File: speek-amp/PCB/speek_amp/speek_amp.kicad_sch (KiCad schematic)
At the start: 71 parts, among them J1 Conn_01x02, J2 R_Tweeter, J3 R_Woofer, J5 L_Tweeter, J6 L_Sub, J7 L_Woofer, U1 TPA3116D2DAD_C2865736, U2 10uH, U3 10uH, U4 XT60, U5 10uH, U6 10uH, U7 PDMTAT068125-151MLU, U8 PDMTAT068125-151MLU, U9 25PX4700MEFC16X25

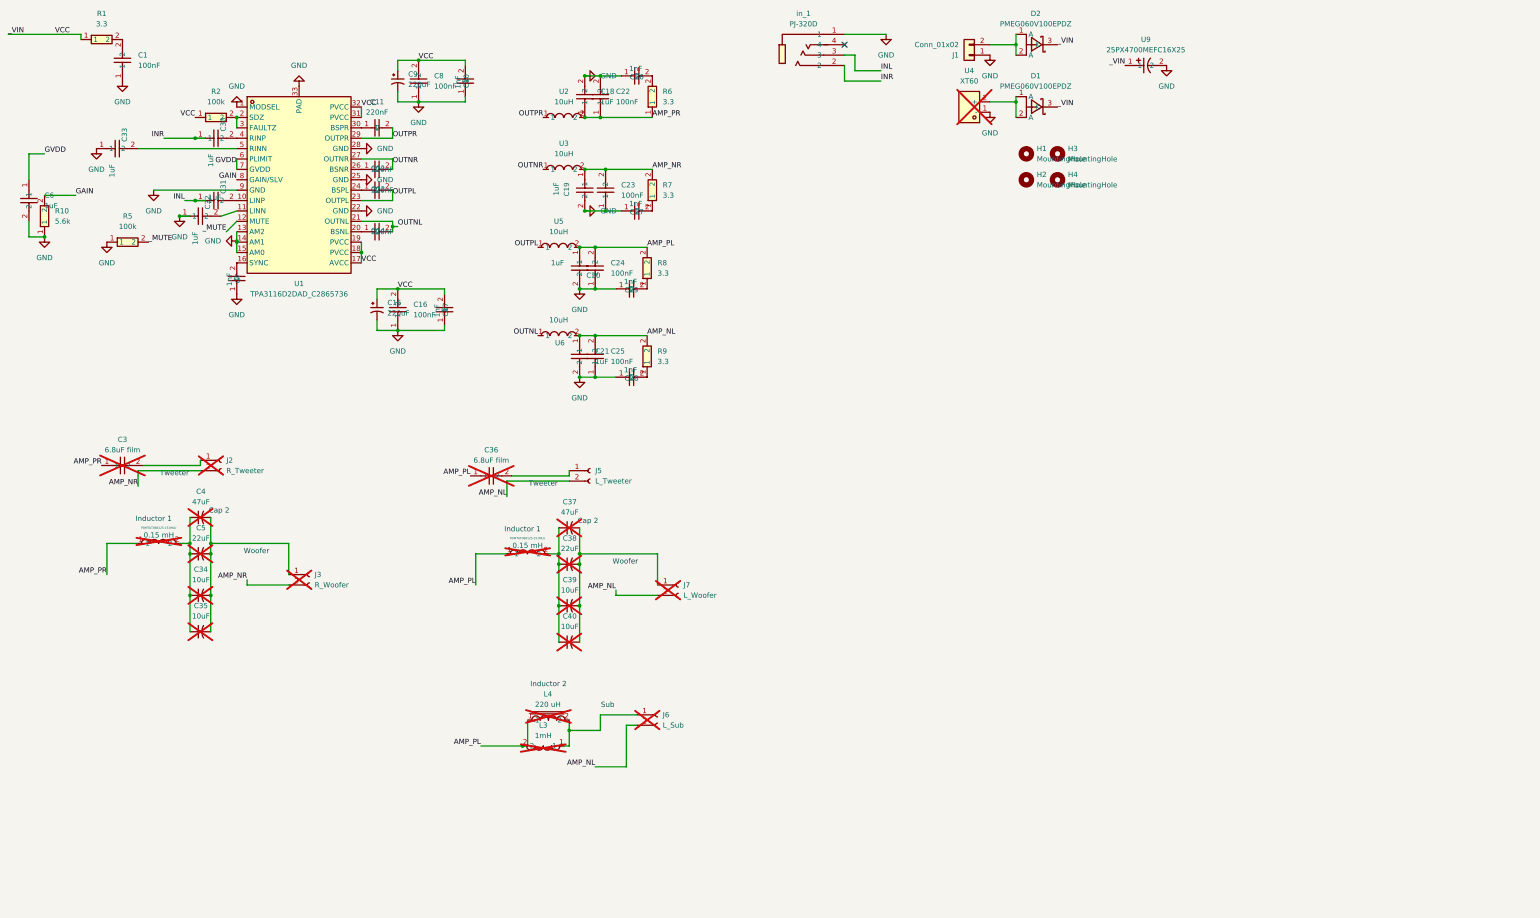
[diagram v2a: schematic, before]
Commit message: [Speek Amp] Schematic rework
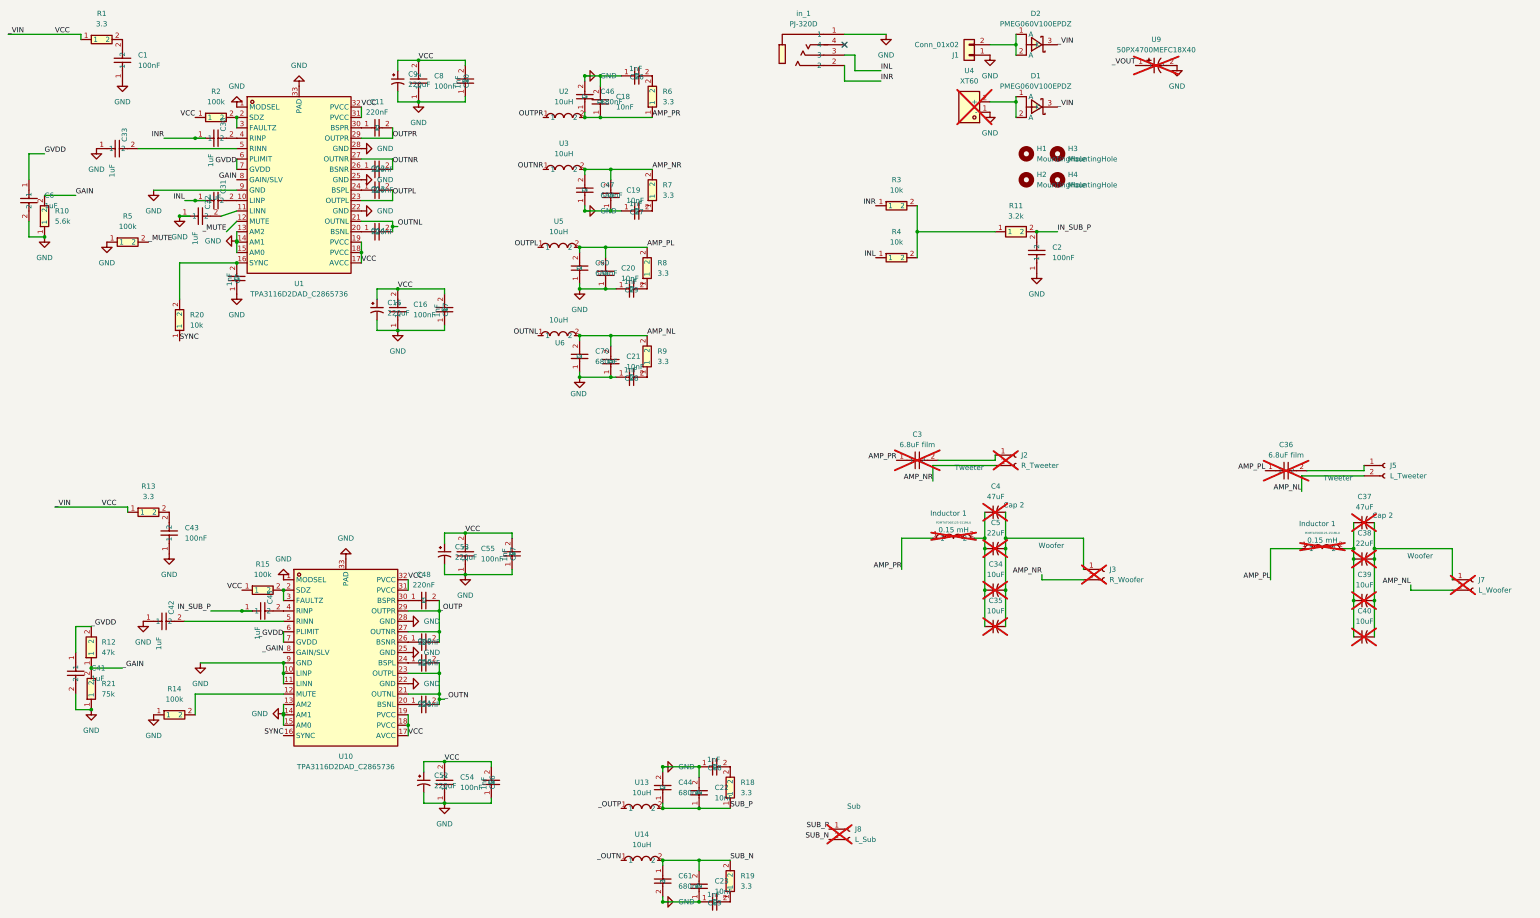
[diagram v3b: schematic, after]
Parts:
- removed C18, C19, C20, C21: 1uF, easyeda2kicad:C0402, symbol lcsc:CGA0402X5R105M100GT
- removed C22, C23, C24, C25: 100nF, easyeda2kicad:C0402, symbol lcsc:CC0402KRX7R7BB104
- removed J6: L_Sub, Connector_PinHeader_2.54mm:PinHeader_1x02_P2.54mm_Vertical, symbol Connector:Conn_01x02_Socket
- removed L3: 1mH, easyeda2kicad:IND-TH_L33.0-W21.0-P15.3-D1.0, symbol lcsc:PDMTAT3321-102MLG
- removed L4: 220 uH, easyeda2kicad:IND-TH_BD22.3-P8.50-D1.2_XR068125TS221MHL8, symbol lcsc:XR068125TS221MHL8
- removed U9: 25PX4700MEFC16X25, easyeda2kicad:CAP-TH_BD16.0-P7.50-D1.2-FD, symbol lcsc:25PX4700MEFC16X25
- added C18, C19, C20, C21, C22, C23: 10nF, easyeda2kicad:C0603, symbol lcsc:CC0603KRX7R9BB103
- added C2: 100nF, easyeda2kicad:C0603, symbol lcsc:CC0603KRX7R9BB104
- added C41, C42, C45: 1uF, easyeda2kicad:C0402, symbol lcsc:CGA0402X5R105M100GT
- added C43, C54, C55: 100nF, easyeda2kicad:C0402, symbol lcsc:CC0402KRX7R7BB104
- added C44, C46, C47, C60, C61, C70: 680nF, easyeda2kicad:C0805, symbol lcsc:CC0805KKX7R9BB684
- added C48, C49, C50, C51: 220nF, easyeda2kicad:C0402, symbol lcsc:CL05B224KO5NNNC
- added C52, C53: 220uF, easyeda2kicad:CAP-SMD_BD8.0-L8.3-W8.3-FD, symbol Device:C_Polarized_Small_US
- added C56, C57, C68, C69: 1nF, easyeda2kicad:C0402, symbol lcsc:CL05B102KB5NNNC
- added J8: L_Sub, Connector_PinHeader_2.54mm:PinHeader_1x02_P2.54mm_Vertical, symbol Connector:Conn_01x02_Socket
- added R11: 3.2k, easyeda2kicad:R0603, symbol lcsc:RT0603BRD073K2L
- added R12: 47k, easyeda2kicad:R0603, symbol lcsc:FRC0603F4702TS
- added R13, R18, R19: 3.3, easyeda2kicad:R0402, symbol lcsc:RC0402FR-073R3L
- added R14, R15: 100k, easyeda2kicad:R0402, symbol lcsc:RC0402FR-07100KL
- added R20, R3, R4: 10k, easyeda2kicad:R0402, symbol lcsc:RC0402FR-0710KL
- added R21: 75k, easyeda2kicad:R0603, symbol lcsc:0603WAF7502T5E
- added U10: TPA3116D2DAD_C2865736, easyeda2kicad:HTSSOP-32_L11.0-W6.1-P0.65-LS8.1-BL, symbol lcsc:TPA3116D2DAD_C2865736
- added U13, U14: 10uH, easyeda2kicad:IND-SMD_L7.2-W6.6_GPSR07X0, symbol lcsc:CYA0630-10UH
- added U9: 50PX4700MEFC18X40, easyeda2kicad:CAP-TH_BD18.0-P7.50-D0.8-FD, symbol lcsc:50PX4700MEFC18X40
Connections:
- net AMP_NL: now also C21.2, C70.2
- net AMP_NR: now also C19.2, C47.2
- net AMP_PL: now also C20.2, C60.2
- net AMP_PR: now also C18.1, C46.1
- net GND: now also C18.2, C19.1, C2.1, C20.1, C21.1, C22.2, C23.1, C41.2, C42.1, C43.1, C44.2, C46.2, C47.1, C52.2, C53.2, C54.1, C55.1, C56.1, C57.1, C60.1, C61.2, C68.1, C69.1, C70.1, R14.1, R21.1, U10.1 (MODSEL), U10.10 (LINP), U10.11 (LINN), U10.13 (AM2), U10.14 (AM1), U10.15 (AM0), U10.22 (GND), U10.25 (GND), U10.28 (GND), U10.33 (PAD), U10.9 (GND), U9.2
- net INL: now also R4.1
- net INR: now also R3.1
- net VCC: now also C52.1, C53.1, C54.2, C55.2, C56.2, C57.2, R13.1, R15.1, U10.17 (AVCC), U10.18 (PVCC), U10.19 (PVCC), U10.31 (PVCC), U10.32 (PVCC)
- net at C7.2, U1.16 (SYNC): now also R20.2
- new net: R11.1, R3.2, R4.2
- new net: C50.1, U10.24 (BSPL)
- new net: C48.1, U10.30 (BSPR)
- new net: C45.2, U10.4 (RINP)
- new net: R14.2, U10.12 (MUTE)
- new net: C68.2, R18.2
- new net: C69.2, R19.1
- new net: C43.2, R13.2
- new net: C51.1, U10.20 (BSNL)
- new net: R15.2, U10.2 (SDZ), U10.3 (FAULTZ)
- new net: C49.1, U10.26 (BSNR)
- new net: C42.2, U10.5 (RINN)
- new net IN_SUB_P: C2.2, C45.1, R11.2
- new net SUB_N: C23.2, C61.1, J8.2 (Pin_2), R19.2, U14.2
- new net SUB_P: C22.1, C44.1, J8.1 (Pin_1), R18.1, U13.2
- new net SYNC: R20.1, U10.16 (SYNC)
- new net _GAIN: R12.1, R21.2, U10.8 (GAIN/SLV)
- new net _GVDD: C41.1, R12.2, U10.6 (PLIMIT), U10.7 (GVDD)
- new net _OUTN: C50.2, C51.2, U10.21 (OUTNL), U10.23 (OUTPL), U14.1
- new net _OUTP: C48.2, C49.2, U10.27 (OUTNR), U10.29 (OUTPR), U13.1
- new net _VOUT: U9.1
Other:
- note removed: "Inductor 2"
- moved on the sheet: C3, C34, C35, C36, C37, C38, C39, C4, C40, C5, J2, J3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

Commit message: [Speek Amp] routing !! [1.25 hours]
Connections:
- net _VOUT is gone; now on net VCC: U9.1
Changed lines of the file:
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@@
+		)
+	)
+	(label "VCC"
+		(at 294.64 27.94 180)
+		(effects
+			(font
+				(size 1.27 1.27)
+			)
+			(justify right bottom)
 		)
 	)
@@
 		)
 	)
-	(label "_VOUT"
-		(at 294.64 27.94 180)
-		(effects
-			(font
-				(size 1.27 1.27)
-			)
-			(justify right bottom)
-		)
-	)

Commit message: e
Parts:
- removed J1: Conn_01x02, Connector_JST:JST_VH_B2P-VH-B_1x02_P3.96mm_Vertical, symbol Connector_Generic:Conn_01x02
- removed J2: R_Tweeter, Connector_PinHeader_2.54mm:PinHeader_1x02_P2.54mm_Vertical, symbol Connector:Conn_01x02_Socket
- removed J3: R_Woofer, Connector_PinHeader_2.54mm:PinHeader_1x02_P2.54mm_Vertical, symbol Connector:Conn_01x02_Socket
- removed J5: L_Tweeter, Connector_PinHeader_2.54mm:PinHeader_1x02_P2.54mm_Vertical, symbol Connector:Conn_01x02_Socket
- removed J7: L_Woofer, Connector_PinHeader_2.54mm:PinHeader_1x02_P2.54mm_Vertical, symbol Connector:Conn_01x02_Socket
- removed J8: L_Sub, Connector_PinHeader_2.54mm:PinHeader_1x02_P2.54mm_Vertical, symbol Connector:Conn_01x02_Socket
- added U11: R_Tweeter, easyeda2kicad:CONN-TH_DB301V-3.5-2P-GN, symbol lcsc:DB301V-3.5-2P-GN
- added U12: R_Woofer, easyeda2kicad:CONN-TH_DB301V-3.5-2P-GN, symbol lcsc:DB301V-3.5-2P-GN
- added U15: L_Tweeter, easyeda2kicad:CONN-TH_DB301V-3.5-2P-GN, symbol lcsc:DB301V-3.5-2P-GN
- added U16: L_Woofer, easyeda2kicad:CONN-TH_DB301V-3.5-2P-GN, symbol lcsc:DB301V-3.5-2P-GN
- added U17: L_Sub, easyeda2kicad:CONN-TH_DB301V-3.5-2P-GN, symbol lcsc:DB301V-3.5-2P-GN
- added U18: J1, easyeda2kicad:CONN-TH_DB301V-3.5-2P-GN, symbol lcsc:DB301V-3.5-2P-GN
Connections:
- net AMP_NL: now also U15.2, U16.2
- net AMP_NR: now also U11.2, U12.2
- net GND: now also U18.1
- net SUB_N: now also U17.2
- net SUB_P: now also U17.1
- net at C34.2, C35.2, C4.2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: now also U12.1
- net at D2.1 (A), D2.2 (A): now also U18.2
- net at C37.2, C38.2, C39.2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: now also U16.1
- net at C3.2: now also U11.1
- net at C36.2: now also U15.1

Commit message: amp
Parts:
- removed D1, D2: PMEG060V100EPDZ, easyeda2kicad:SOT1289_L5.8-W4.4-LS6.5-RD, symbol lcsc:PMEG060V100EPDZ
- C1, C16, C43, C54, C55, C8: symbol lcsc:CC0402KRX7R7BB104 -> lcsc:CL05B104KB54PNC; LCSC Part C60474 -> C307331; MPN CC0402KRX7R7BB104 -> CL05B104KB54PNC
- C10, C17, C26, C27, C28, C29, C56, C57, C68, C69, C7: symbol lcsc:CL05B102KB5NNNC -> lcsc:0402B102K500NT; LCSC Part C14442 -> C1523; MPN CL05B102KB5NNNC -> 0402B102K500NT
- C18, C19, C20, C21, C22, C23: symbol lcsc:CC0603KRX7R9BB103 -> lcsc:0603B103K500NT; LCSC Part C100042 -> C57112; MPN CC0603KRX7R9BB103 -> 0603B103K500NT
- C30, C31, C32, C33, C41, C42, C45, C6: symbol lcsc:CGA0402X5R105M100GT -> lcsc:CL05A105KA5NQNC; LCSC Part C22399609 -> C52923; MPN CGA0402X5R105M100GT -> CL05A105KA5NQNC
- R12: symbol lcsc:FRC0603F4702TS -> lcsc:0603WAF4702T5E; LCSC Part C2907042 -> C25819; MPN FRC0603F4702TS -> 0603WAF4702T5E
- R14, R15, R2, R5: symbol lcsc:RC0402FR-07100KL -> lcsc:0402WGF1003TCE; LCSC Part C60491 -> C25741; MPN RC0402FR-07100KL -> 0402WGF1003TCE
- R20, R3, R4: symbol lcsc:RC0402FR-0710KL -> lcsc:0402WGF1002TCE; LCSC Part C60490 -> C25744; MPN RC0402FR-0710KL -> 0402WGF1002TCE
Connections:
- net VCC: now also U18.2, U4.2 (+)
